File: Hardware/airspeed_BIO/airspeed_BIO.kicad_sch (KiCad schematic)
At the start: 0 parts

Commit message: Power management system save
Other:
- added sheet connector (connector.kicad_sch)
- added sheet power (power.kicad_sch)
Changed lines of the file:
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@@
 		(comment 1 "design by Chen")
+	)
+	(sheet
+		(at 95.25 41.91)
+		(size 30.48 78.74)
+		(exclude_from_sim no)
+		(in_bom yes)
+		(on_board yes)
+		(dnp no)
+		(fields_autoplaced yes)
+		(stroke
+			(width 0.1524)
+			(type solid)
+		)
+		(fill
+			(color 0 0 0 0.0000)
+		)
+		(property "Sheetname" "connector"
+			(at 95.25 41.1984 0)
+			(effects
+				(font
+					(size 1.27 1.27)
+				)
+				(justify left bottom)
+			)
+		)
+		(property "Sheetfile" "connector.kicad_sch"
+			(at 95.25 121.2346 0)
+			(effects
+				(font
+					(size 1.27 1.27)
+				)
+				(justify left top)
+			)
+		)
+		(instances
+			(project "airspeed_BIO"
+				(path "/6ddcf4fe-9e51-4114-8222-5fc3f810c12a"
+					(page "3")
+				)
+			)
+		)
+	)
+	(sheet
+		(at 43.18 43.18)
+		(size 31.75 19.05)
+		(exclude_from_sim no)
+		(in_bom yes)
+		(on_board yes)
+		(dnp no)
+		(fields_autoplaced yes)
+		(stroke
+			(width 0.1524)
+			(type solid)
+		)
+		(fill
+			(color 0 0 0 0.0000)
+		)
+		(property "Sheetname" "power"
+			(at 43.18 42.4684 0)
+			(effects
+				(font
+					(size 1.27 1.27)
+				)
+				(justify left bottom)
+			)
+		)
+		(property "Sheetfile" "power.kicad_sch"
+			(at 43.18 62.8146 0)
+			(effects
+				(font
+					(size 1.27 1.27)
+				)
+				(justify left top)
+			)
+		)
+		(instances
+			(project "airspeed_BIO"
+				(path "/6ddcf4fe-9e51-4114-8222-5fc3f810c12a"
+					(page "2")
+				)
+			)
+		)
 	)
 	(sheet_instances

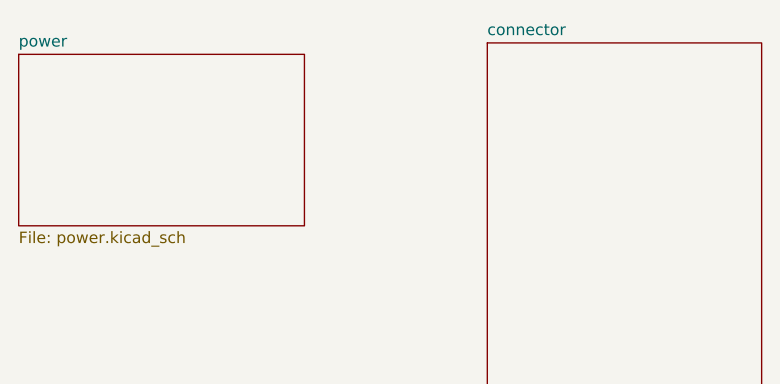
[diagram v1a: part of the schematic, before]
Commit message: power end didn't set I limit
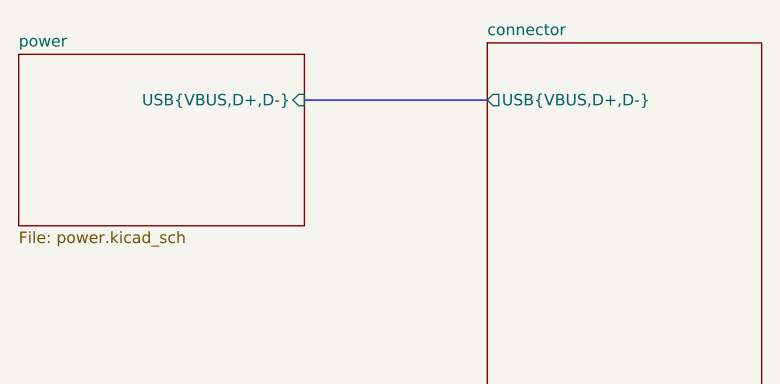
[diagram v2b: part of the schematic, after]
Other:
- sheet connector ports: added USB{VBUS,D+,D-}; removed none
- sheet power ports: added USB{VBUS,D+,D-}; removed none
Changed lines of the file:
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@@
 		(comment 1 "design by Chen")
+	)
+	(bus
+		(pts
+			(xy 74.93 48.26) (xy 95.25 48.26)
+		)
+		(stroke
+			(width 0)
+			(type default)
+		)
 	)
 	(sheet
@@
 				)
 				(justify left top)
+			)
+		)
+		(pin "USB{VBUS,D+,D-}" output
+			(at 95.25 48.26 180)
+			(effects
+				(font
+					(size 1.27 1.27)
+				)
+				(justify left)
 			)
 		)
@@
 			)
 		)
+		(pin "USB{VBUS,D+,D-}" input
+			(at 74.93 48.26 0)
+			(effects
+				(font
+					(size 1.27 1.27)
+				)
+				(justify right)
+			)
+		)

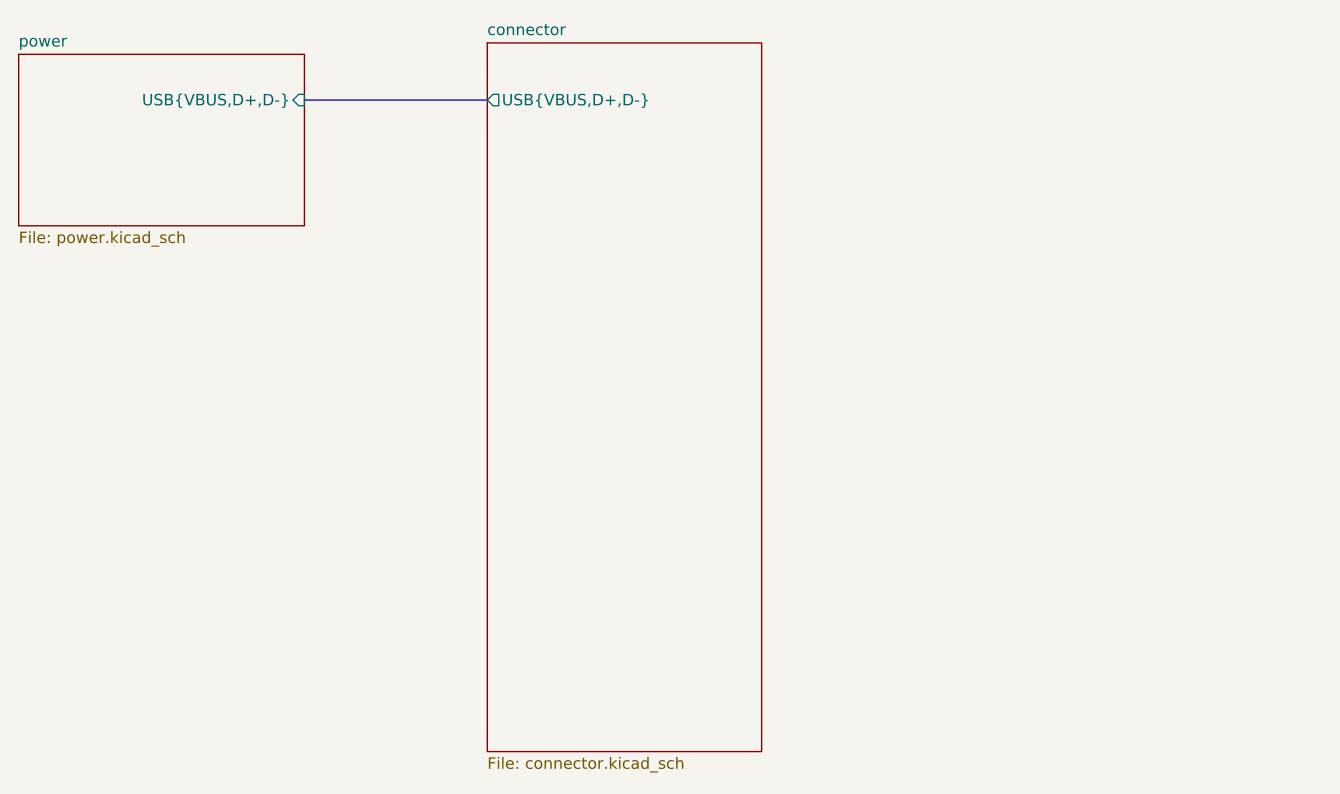
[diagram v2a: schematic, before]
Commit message: add mcu audio
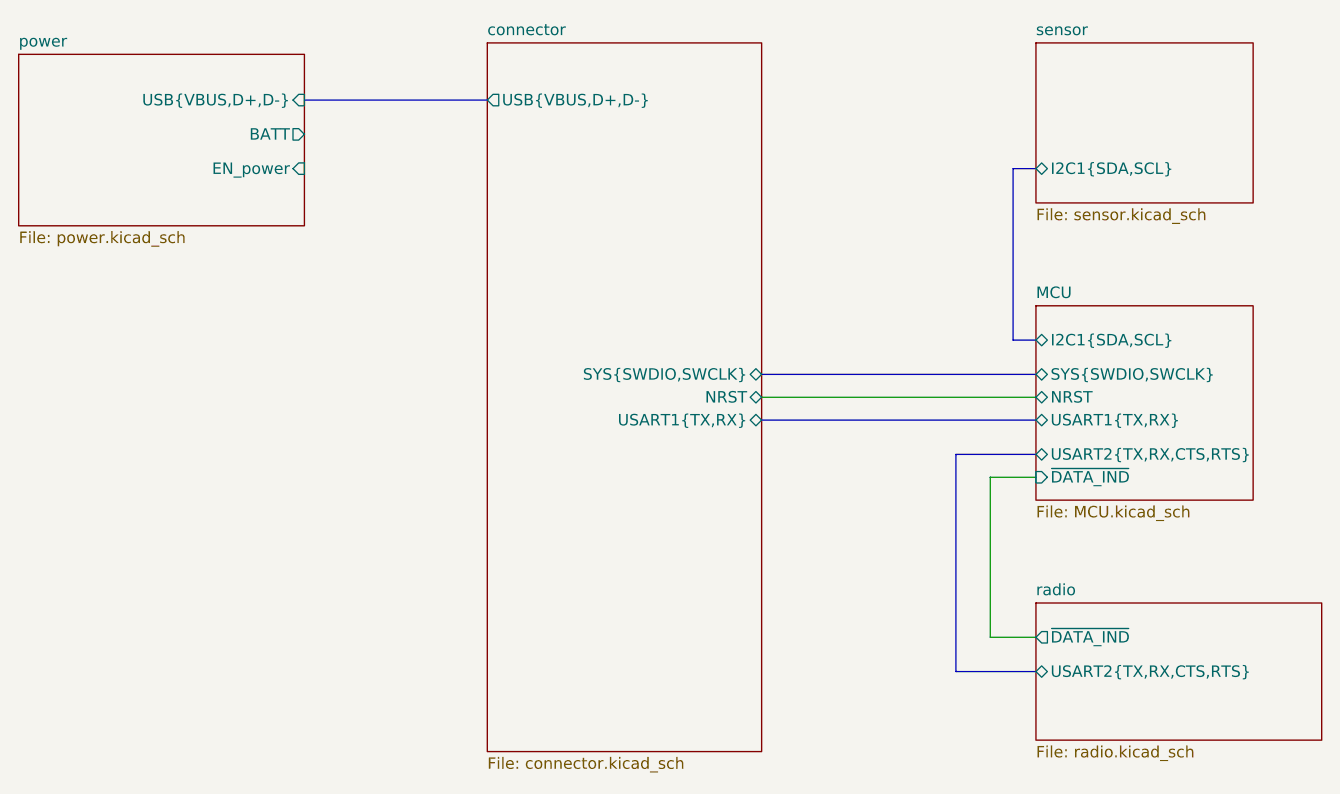
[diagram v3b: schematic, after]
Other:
- added sheet MCU (MCU.kicad_sch)
- added sheet radio (radio.kicad_sch)
- added sheet sensor (sensor.kicad_sch)
- sheet connector ports: added NRST, SYS{SWDIO,SWCLK}, USART1{TX,RX}; removed none
- sheet power ports: added BATT, EN_power; removed none
- company: (none) -> Taipei Tech Racing

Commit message: set Ilimit and set footprint
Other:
- sheet connector ports: added BATT, EN_power, VCCmp; removed none
- sheet power ports: added VCCpm; removed none
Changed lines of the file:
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@@
+		)
+	)
+	(wire
+		(pts
+			(xy 74.93 58.42) (xy 95.25 58.42)
+		)
+		(stroke
+			(width 0)
+			(type default)
 		)
 	)
@@
 		)
 	)
+	(wire
+		(pts
+			(xy 74.93 52.07) (xy 95.25 52.07)
+		)
+		(stroke
+			(width 0)
+			(type default)
+		)
+	)
 	(bus
 		(pts
@@
 		(pts
 			(xy 125.73 78.74) (xy 156.21 78.74)
+		)
+		(stroke
+			(width 0)
+			(type default)
+		)
+	)
+	(wire
+		(pts
+			(xy 74.93 55.88) (xy 95.25 55.88)
 		)
 		(stroke
@@
 			)
 		)
+		(pin "BATT" output
+			(at 95.25 52.07 180)
+			(effects
+				(font
+					(size 1.27 1.27)
+				)
+				(justify left)
+			)
+		)
+		(pin "EN_power" output
+			(at 95.25 55.88 180)
+			(effects
+				(font
+					(size 1.27 1.27)
+				)
+				(justify left)
+			)
+		)
+		(pin "VCCmp" input
+			(at 95.25 58.42 180)
+			(effects
+				(font
+					(size 1.27 1.27)
+				)
+				(justify left)
+			)
+		)
 		(instances
 			(project "airspeed_BIO"
@@
 			(effects
 				(font
+					(size 1.27 1.27)
+				)
+				(justify right)
+			)
+		)
+		(pin "VCCpm" output
+			(at 74.93 58.42 0)
+			(effects
+				(font

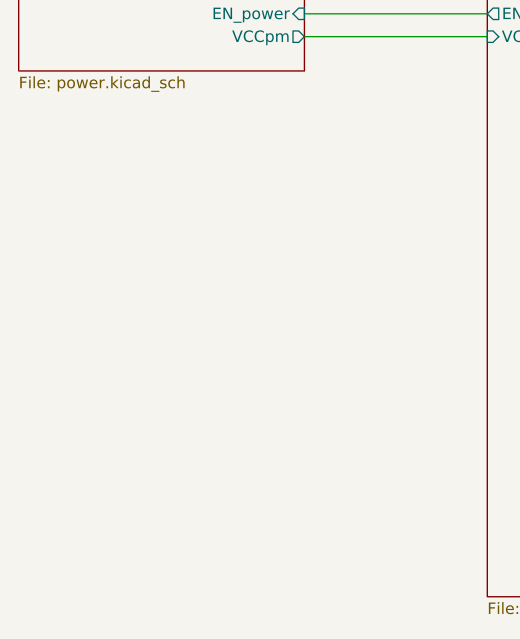
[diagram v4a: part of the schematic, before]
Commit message: layout and fix Schematic
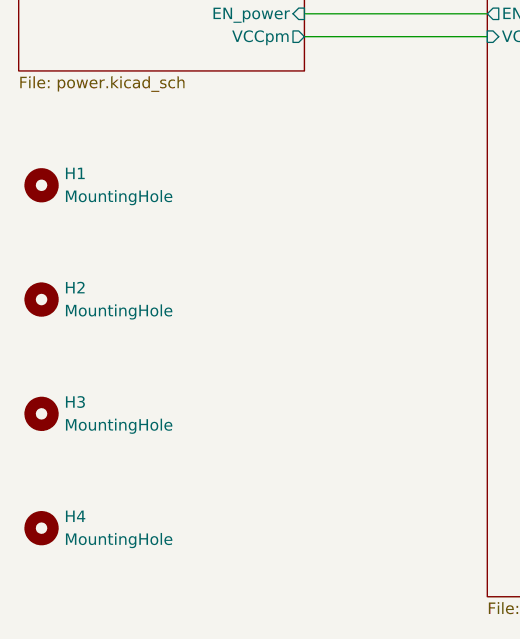
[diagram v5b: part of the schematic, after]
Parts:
- added H1, H2, H3, H4: MountingHole, MountingHole:MountingHole_2.2mm_M2, symbol Mechanical:MountingHole
